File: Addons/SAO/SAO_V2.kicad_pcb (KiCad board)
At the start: 2 copper layers, 90 x 21.2 mm, 15 parts, among them J1 Conn_02x03, J2 Conn_02x03, J3 Conn_02x03, J5 Conn_01x10_Pin, J6 Conn_01x08_Pin

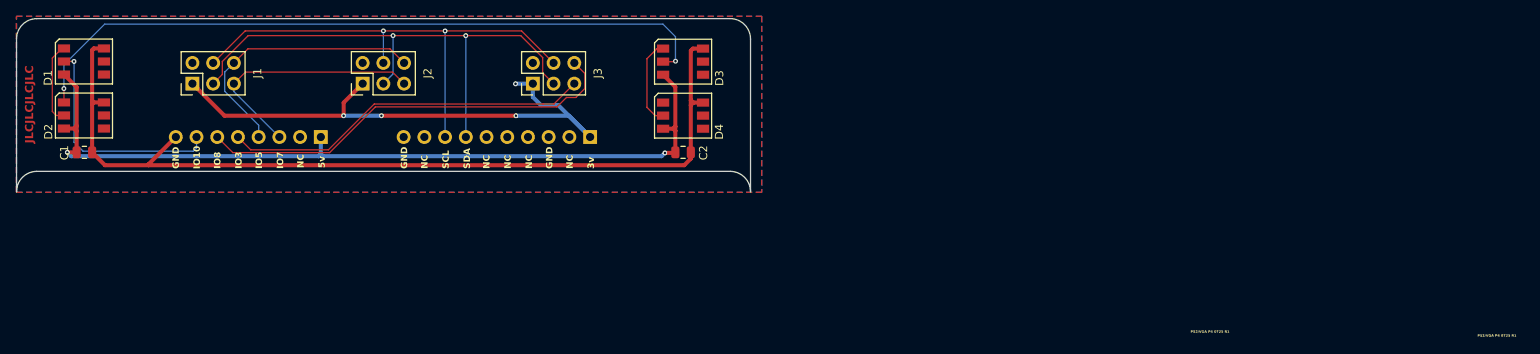
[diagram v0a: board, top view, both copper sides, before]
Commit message: Flipped SAO connectors, to match v1.69bis spec
Also
- Re-routed connections to the SAO connectors
- Teaked clearance for fill and moved a few traces for better GND and VCC coverage
- Changed 3v to 3v3 silkscreen on connector to badge
- Changed 3D model to be badge side keyed SAO connector

Signed-off-by: Thomas Flummer <tf@flummer.net>
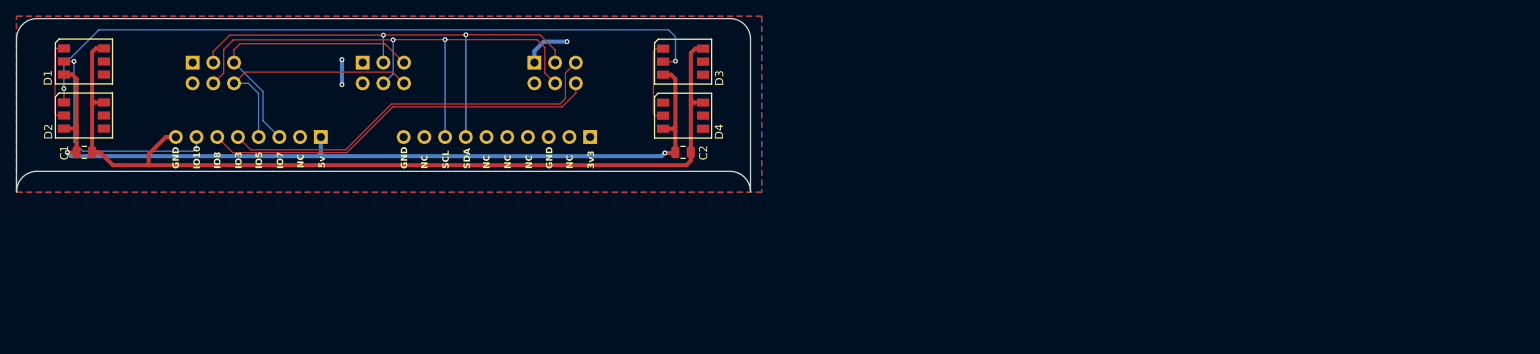
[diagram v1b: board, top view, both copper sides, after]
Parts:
- J1, J2, J3: moved to B.Cu
- moved J3 2.59 mm to (103.5, 141.9), turned to -90 degrees
- moved J1 2.58 mm to (61.6, 141.9), turned to -90 degrees
- moved J2 2.58 mm to (82.4, 141.9), turned to -90 degrees
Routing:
- net +3.3V: track 69.2 -> 8.97 mm, vias 4 -> 3
- net I2C2.SCL: track 61.9 -> 67.7 mm
- net I2C2.SDA: track 67.4 -> 62.4 mm
- net GPIO7: track 30.9 -> 35.2 mm
- net GPIO8: track 52.8 -> 49.0 mm
- net GPIO3: track 45.3 -> 48.3 mm
- net GPIO5: track 33.6 -> 30.9 mm
- net +5V: track 103.9 -> 105.0 mm
- net Net-(D3-DOUT): track 9.88 -> 9.30 mm
- net Net-(D2-DOUT): track 87.3 -> 86.8 mm
- net GND: track 112.1 -> 112.6 mm
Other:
- board text added: "3v3"
- board text removed: "3v"
- board text removed: "JLCJLCJLCJLC"
- board text removed: "PS2/VGA P4 0725 R1"
